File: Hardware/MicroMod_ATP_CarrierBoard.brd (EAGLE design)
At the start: 83.8 x 55.9 mm, 67 parts, among them J19 QWIIC_RIGHT_ANGLE, J2 JTAG, J20 QWIIC_RIGHT_ANGLE, J21 1X04_SMD_STRAIGHT_COMBO, J23 1X04_SMD_STRAIGHT_COMBO, J4 USB_A_SMT_FEMALE, J6 MICROMOD-2222-C, J8 1X04_SMD_STRAIGHT_COMBO, U5 AP7361C-33

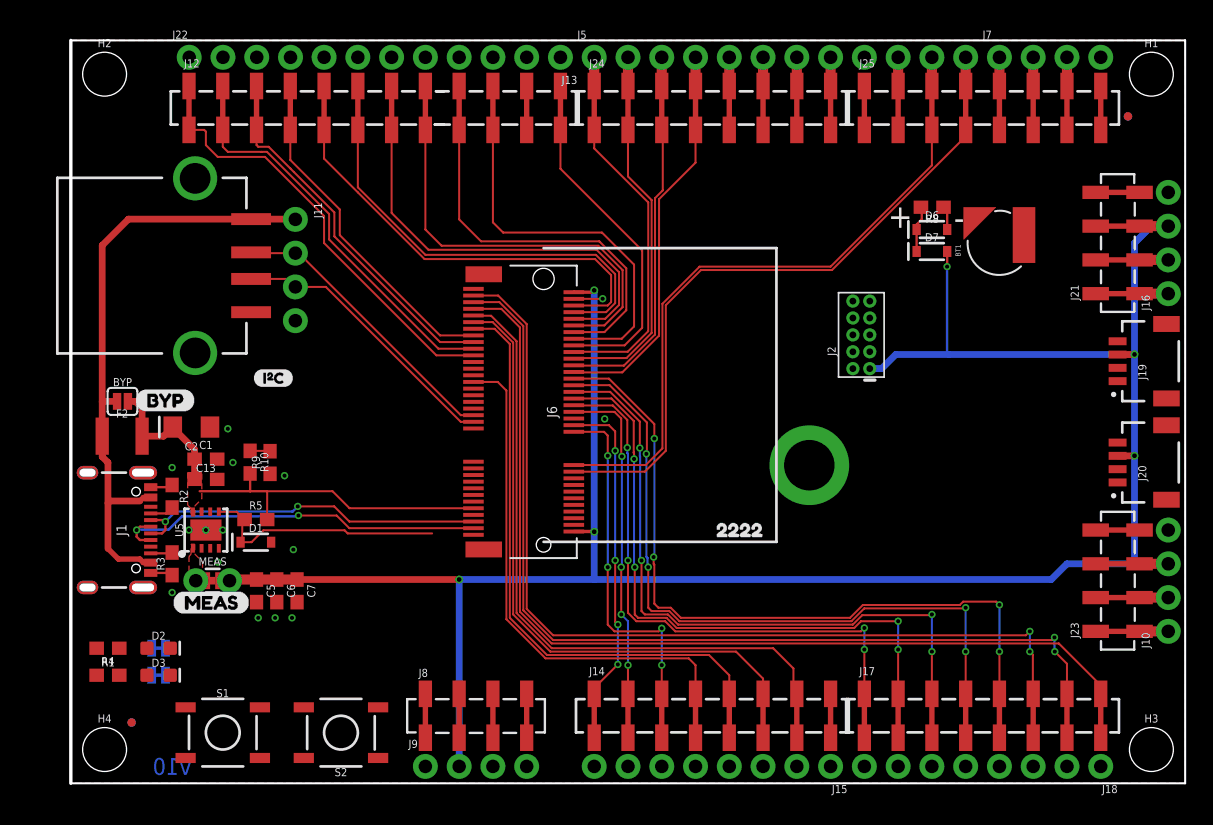
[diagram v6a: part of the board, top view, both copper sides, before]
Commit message: Routes Serial, I2C, and CAN lines
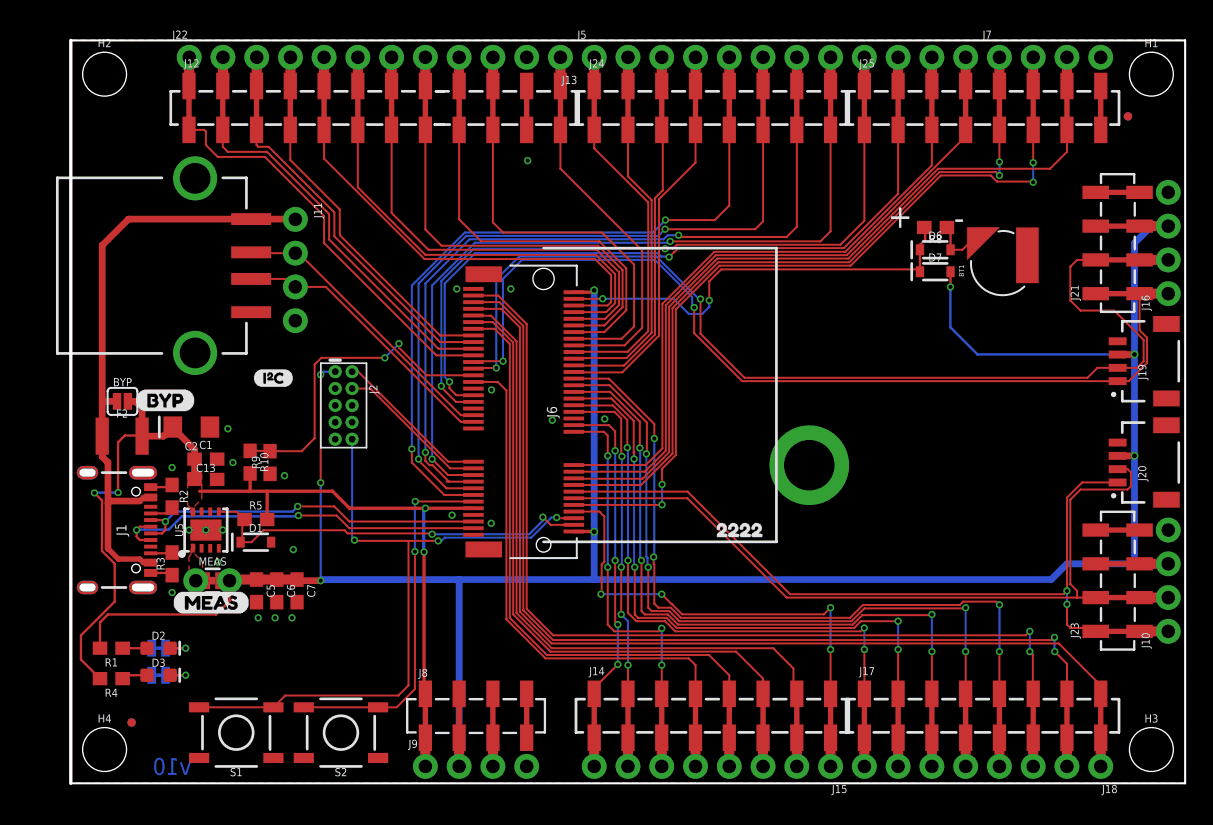
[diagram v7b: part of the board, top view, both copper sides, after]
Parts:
- moved J2 39.3 mm to (20.5, 28.4), turned to 270 degrees
- moved BT1 1.55 mm to (70.1, 39.1)
- moved D6 1.55 mm to (65.0, 40.1)
- moved D7 1.55 mm to (65.0, 38.5)
- moved R8 1.55 mm to (65.0, 41.8)
- moved S1 1.02 mm to (12.4, 3.81), turned to 180 degrees
- moved R4 0.36 mm to (3.05, 7.87), turned to 180 degrees
- moved R1 0.25 mm to (3.05, 10.2)
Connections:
- net CAN_RXI: now also J25.1, J25.1@2, J5.9; no longer J25.2, J25.2@2, J5.10
- net CAN_TXO: now also J25.2, J25.2@2, J5.10; no longer J25.1, J25.1@2, J5.9
- net CTS1: now also J24.6, J24.6@2, J5.6; no longer J24.5, J24.5@2, J5.5
- net RTS1: now also J24.5, J24.5@2, J5.5; no longer J24.6, J24.6@2, J5.6
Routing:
- net SDA1: track 2.16 -> 78.8 mm, vias 0 -> 2
- net SCL1: track 2.16 -> 70.9 mm, vias 0 -> 2
- net SCL: track 2.16 -> 59.3 mm, vias 0 -> 2
- net SDA: track 2.16 -> 59.2 mm
- net D0: track 2.16 -> 59.1 mm, vias 0 -> 4
- net RX1: track 1.85 -> 57.8 mm, vias 0 -> 2
- net D1: track 2.16 -> 57.5 mm
- net TX1: track 1.85 -> 56.8 mm, vias 0 -> 2
- net CAN_TXO: track 0.00 -> 53.4 mm, vias 0 -> 2
- net CTS1: track 1.57 -> 54.9 mm, vias 0 -> 2
- net !RESET: track 0.00 -> 52.3 mm, vias 0 -> 3
- net CAN_RXI: track 1.27 -> 53.3 mm, vias 0 -> 2
- net I2C_!INT: track 2.16 -> 53.9 mm, vias 0 -> 2
- net RTS1: track 1.85 -> 52.6 mm, vias 0 -> 2
- net VIN: track 35.2 -> 75.0 mm, vias 0 -> 4
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
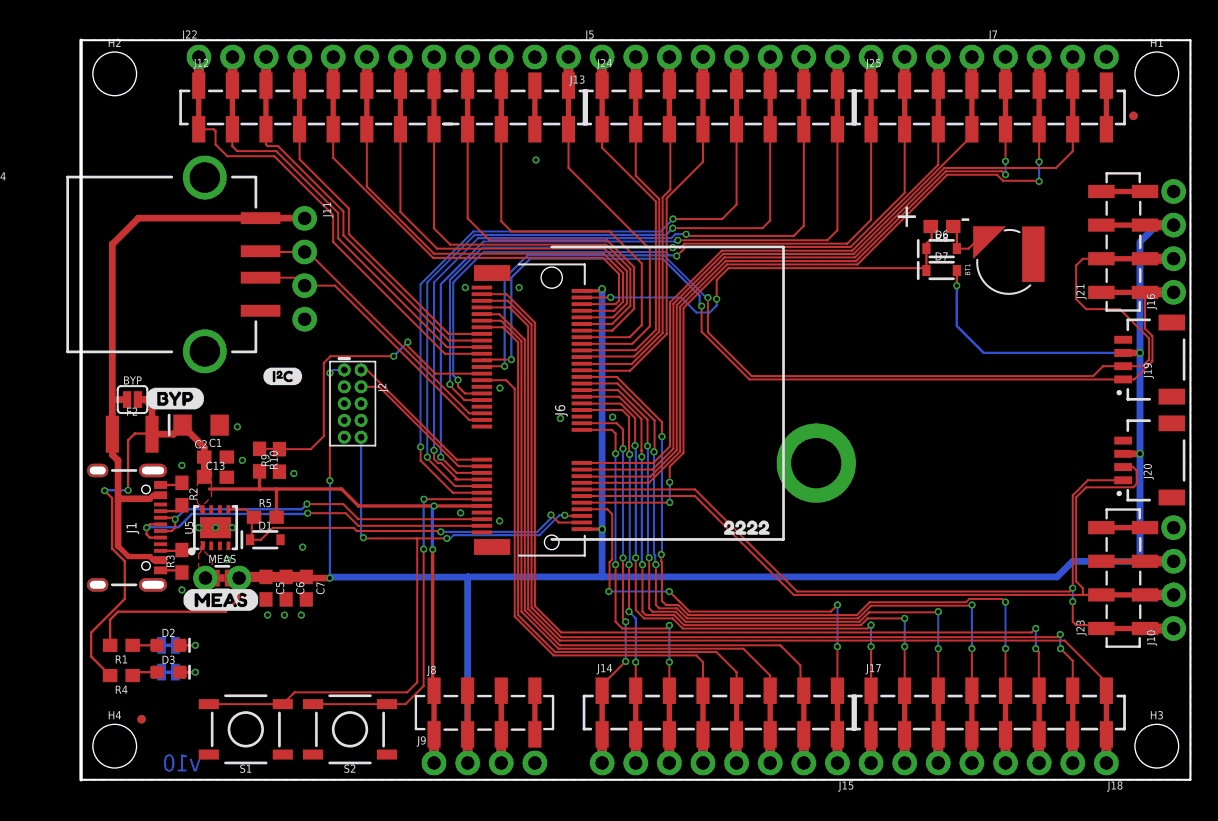
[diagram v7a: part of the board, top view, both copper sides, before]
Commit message: Reorders the "G#" lines and moves traces so that they hit at 90 degrees
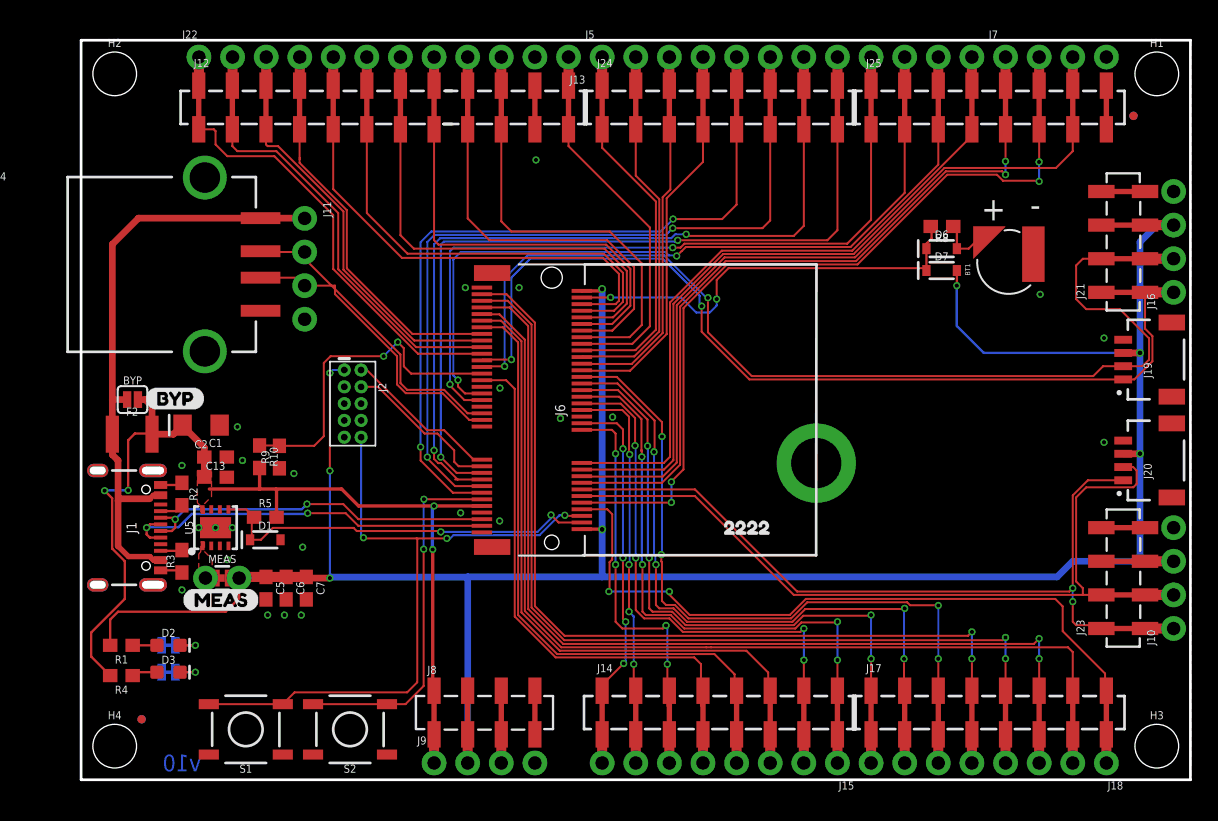
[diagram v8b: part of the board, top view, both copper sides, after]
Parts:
- removed U$42: (no value), SparkFun-Buzzard:I2C_32
- moved R10 0.25 mm to (13.5, 24.4)
- moved R9 0.25 mm to (15.0, 24.4)
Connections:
- net SD_!CS! renamed !CS!
- net G0: now also J14.7, J14.7@2, J15.2; no longer J17.1, J17.1@2, J18.8
- net G1: now also J14.8, J14.8@2, J15.1; no longer J17.2, J17.2@2, J18.7
- net G11: now also J17.8, J17.8@2, J18.1; no longer J14.8, J14.8@2, J15.1
- net G2: now also J17.1, J17.1@2, J18.8; no longer J17.3, J17.3@2, J18.6
- net G3: now also J17.2, J17.2@2, J18.7; no longer J17.4, J17.4@2, J18.5
- net G4: now also J17.3, J17.3@2, J18.6; no longer J17.5, J17.5@2, J18.4
- net G5: now also J17.4, J17.4@2, J18.5; no longer J17.6, J17.6@2, J18.3
- net G6: now also J17.5, J17.5@2, J18.4; no longer J17.7, J17.7@2, J18.2
- net G7: now also J17.6, J17.6@2, J18.3; no longer J17.8, J17.8@2, J18.1
- net G8: now also J17.7, J17.7@2, J18.2; no longer J14.7, J14.7@2, J15.2
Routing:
- net G8: track 50.9 -> 72.0 mm
- net G11: track 34.8 -> 53.6 mm, vias 4 -> 2
- net G0: track 45.3 -> 39.1 mm
- net G2: track 51.6 -> 45.4 mm
- net G1: track 48.7 -> 42.4 mm
- net G3: track 54.7 -> 48.5 mm
- net G4: track 57.6 -> 51.4 mm
- net G6: track 74.4 -> 68.7 mm
- net G5: track 71.8 -> 66.7 mm
- net G7: track 73.6 -> 70.9 mm, vias 0 -> 2
- net RTS1: track 52.6 -> 54.4 mm
- net CTS1: track 54.9 -> 56.7 mm
- net RX1: track 57.8 -> 59.6 mm
- net TX1: track 56.8 -> 58.4 mm
- net USBHOST_P: track 21.2 -> 22.8 mm
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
